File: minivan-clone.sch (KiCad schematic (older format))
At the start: 15 parts, among them CON101 HRO-TYPE-C-31-M-12, SW101 SW_PUSH, U101 ATMEGA32U2, X101 XTAL

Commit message: done work on mcu and started on matrix
done work on mcu and started on matrix
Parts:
- added C110: C, symbol keyboard_parts:C
- added CON101: CONN_3X2, symbol keyboard_parts:CONN_3X2
- added R102: 10K, symbol keyboard_parts:R
- added R103, R104: 22R, symbol keyboard_parts:R
- added R105, R106: 5K1, symbol keyboard_parts:R
- CON101: footprint (none) -> Type-C:HRO-TYPE-C-31-M-12-HandSoldering
- R101: value R -> 10K
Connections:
- net labels added: DN, DP, MISO, MOSI, PB0, PB1, PB2, PB3, PB4, PB5, PB6, PB7, PC2, PC4, PC5, PC6, PC7, PD0, PD1, PD2, PD3, PD4, PD5, PD6, RST, RX, SCK, TX
- wire segments 23 -> 61
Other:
- note added: "Dubbelkolla så denna ska va pulldown\n"
- moved on the sheet: C109, PTC101, R101, SW101

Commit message: started doing layout
started doing layout
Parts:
- removed X101: XTAL, symbol keyboard_parts:XTAL
- added D148: PRTR5V0U2X, Package_TO_SOT_SMD:SOT-143, symbol Power_Protection:PRTR5V0U2X
- added X101: XTAL_GND, keyboard_parts:FA-238, symbol keyboard_parts:XTAL_GND
- C101, C102, C103, C104, C109: value C -> 0,1uF; footprint (none) -> keyboard_parts:C_1608_rev2
- C105, C106: value C -> 4,7uF; footprint (none) -> keyboard_parts:C_3216_rev2
- C107, C108: value C -> C_xtal; footprint (none) -> keyboard_parts:C_1608_rev2
- C110: value C -> 1uF; footprint (none) -> keyboard_parts:C_3216_rev2
- CON102: renamed from CON101; footprint (none) -> keyboard_parts:AVR_ICSP_3x2
- PTC101: footprint (none) -> keyboard_parts:C_3216_rev2
- R101, R102, R103, R104, R105, R106: footprint (none) -> keyboard_parts:R_1608_rev2
- SW101: footprint (none) -> keyboard_parts:SW_ALPS_SKRP
- U101: footprint (none) -> keyboard_parts:QFP32
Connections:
- net labels added: D+, D-
- wire segments 61 -> 82
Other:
- note added: "Dubbelkolla kapacitans"
- note removed: "Dubbelkolla så denna ska va pulldown\n"
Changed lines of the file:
@@
 F 0 "U101" H 7925 2837 60  0000 C CNN
 F 1 "ATMEGA32U2" H 7925 2731 60  0000 C CNN
-F 2 "" H 7900 1500 60  0000 C CNN
+F 2 "keyboard_parts:QFP32" H 7900 1500 60  0001 C CNN
 F 3 "" H 7900 1500 60  0000 C CNN
 	1    7900 1800
-	1    0    0    -1
-$EndComp
-$Comp
-L keyboard_parts:XTAL X101
-U 1 1 5D1B97DB
-P 5050 1300
-F 0 "X101" H 5050 1592 60  0000 C CNN
-F 1 "XTAL" H 5050 1486 60  0000 C CNN
-F 2 "" H 5050 1300 60  0000 C CNN
-F 3 "" H 5050 1300 60  0000 C CNN
-	1    5050 1300
 	1    0    0    -1
 $EndComp
@@
 F 0 "SW101" H 10600 2105 50  0000 C CNN
 F 1 "SW_PUSH" H 10600 2014 50  0000 C CNN
-F 2 "" H 10600 1850 60  0000 C CNN
+F 2 "keyboard_parts:SW_ALPS_SKRP" H 10600 1850 60  0001 C CNN
 F 3 "" H 10600 1850 60  0000 C CNN
 	1    10600 1850
@@
 F 0 "R101" H 10371 1596 50  0000 L CNN
 F 1 "10K" H 10371 1505 50  0000 L CNN
-F 2 "" H 10300 1550 60  0000 C CNN
+F 2 "keyboard_parts:R_1608_rev2" H 10300 1550 60  0001 C CNN
 F 3 "" H 10300 1550 60  0000 C CNN
 	1    10300 1550
@@
 P 9100 5700
 F 0 "C102" H 9230 5746 50  0000 L CNN
-F 1 "C" H 9230 5655 50  0000 L CNN
-F 2 "" H 9100 5700 60  0000 C CNN
+F 1 "0,1uF" H 9230 5655 50  0000 L CNN
+F 2 "keyboard_parts:C_1608_rev2" H 9100 5700 60  0001 C CNN
 F 3 "" H 9100 5700 60  0000 C CNN
 	1    9100 5700
@@
 P 8500 5700
 F 0 "C101" H 8630 5746 50  0000 L CNN
-F 1 "C" H 8630 5655 50  0000 L CNN
-F 2 "" H 8500 5700 60  0000 C CNN
+F 1 "0,1uF" H 8630 5655 50  0000 L CNN
+F 2 "keyboard_parts:C_1608_rev2" H 8500 5700 60  0001 C CNN
 F 3 "" H 8500 5700 60  0000 C CNN
 	1    8500 5700
@@
 P 9600 5700
 F 0 "C103" H 9730 5746 50  0000 L CNN
-F 1 "C" H 9730 5655 50  0000 L CNN
-F 2 "" H 9600 5700 60  0000 C CNN
+F 1 "0,1uF" H 9730 5655 50  0000 L CNN
+F 2 "keyboard_parts:C_1608_rev2" H 9600 5700 60  0001 C CNN
 F 3 "" H 9600 5700 60  0000 C CNN
 	1    9600 5700
@@
 P 10100 5700
 F 0 "C104" H 10230 5746 50  0000 L CNN
-F 1 "C" H 10230 5655 50  0000 L CNN
-F 2 "" H 10100 5700 60  0000 C CNN
+F 1 "0,1uF" H 10230 5655 50  0000 L CNN
+F 2 "keyboard_parts:C_1608_rev2" H 10100 5700 60  0001 C CNN
 F 3 "" H 10100 5700 60  0000 C CNN
 	1    10100 5700
@@
 P 7350 5700
 F 0 "C105" H 7480 5746 50  0000 L CNN
-F 1 "C" H 7480 5655 50  0000 L CNN
-F 2 "" H 7350 5700 60  0000 C CNN
+F 1 "4,7uF" H 7480 5655 50  0000 L CNN
+F 2 "keyboard_parts:C_3216_rev2" H 7350 5700 60  0001 C CNN
 F 3 "" H 7350 5700 60  0000 C CNN
 	1    7350 5700
@@
 P 6200 5700
 F 0 "C106" H 6330 5746 50  0000 L CNN
-F 1 "C" H 6330 5655 50  0000 L CNN
-F 2 "" H 6200 5700 60  0000 C CNN
+F 1 "4,7uF" H 6330 5655 50  0000 L CNN
+F 2 "keyboard_parts:C_3216_rev2" H 6200 5700 60  0001 C CNN
 F 3 "" H 6200 5700 60  0000 C CNN
 	1    6200 5700
@@
 P 4750 1600
 F 0 "C107" H 4880 1646 50  0000 L CNN
-F 1 "C" H 4880 1555 50  0000 L CNN
-F 2 "" H 4750 1600 60  0000 C CNN
+F 1 "C_xtal" H 4880 1555 50  0000 L CNN
+F 2 "keyboard_parts:C_1608_rev2" H 4750 1600 60  0001 C CNN
 F 3 "" H 4750 1600 60  0000 C CNN
 	1    4750 1600
@@
 P 5350 1600
 F 0 "C108" H 5480 1646 50  0000 L CNN
-F 1 "C" H 5480 1555 50  0000 L CNN
-F 2 "" H 5350 1600 60  0000 C CNN
+F 1 "C_xtal" H 5480 1555 50  0000 L CNN
+F 2 "keyboard_parts:C_1608_rev2" H 5350 1600 60  0001 C CNN
 F 3 "" H 5350 1600 60  0000 C CNN
 	1    5350 1600
 	1    0    0    -1
 $EndComp
-Wire Wire Line
-	5350 1300 5350 1400
-Wire Wire Line
-	4750 1300 4750 1400
 $Comp
 L keyboard_parts:C C109
@@
 P 10300 2150
 F 0 "C109" H 10430 2196 50  0000 L CNN
-F 1 "C" H 10430 2105 50  0000 L CNN
-F 2 "" H 10300 2150 60  0000 C CNN
+F 1 "0,1uF" H 10430 2105 50  0000 L CNN
+F 2 "keyboard_parts:C_1608_rev2" H 10300 2150 60  0001 C CNN
 F 3 "" H 10300 2150 60  0000 C CNN
 	1    10300 2150
@@
 	6850 1050 4750 1050
 Wire Wire Line
-	4750 1050 4750 1300
-Connection ~ 4750 1300
-Wire Wire Line
 	6850 1150 5350 1150
-Wire Wire Line
-	5350 1150 5350 1300
-Connection ~ 5350 1300
 Connection ~ 8500 5900
 Wire Wire Line
@@
 F 0 "R102" H 5921 2546 50  0000 L CNN
 F 1 "10K" H 5921 2455 50  0000 L CNN
-F 2 "" H 5850 2500 60  0000 C CNN
+F 2 "keyboard_parts:R_1608_rev2" H 5850 2500 60  0001 C CNN
 F 3 "" H 5850 2500 60  0000 C CNN
 	1    5850 2500
@@
 	1    0    0    -1
 $EndComp
-Text Notes 5200 2900 0    50   ~ 0
-Dubbelkolla så denna ska va pulldown\n
 $Comp
 L keyboard_parts:+5V #PWR0109
@@
 P 9900 1350
 F 0 "C110" H 10030 1396 50  0000 L CNN
-F 1 "C" H 10030 1305 50  0000 L CNN
-F 2 "" H 9900 1350 60  0000 C CNN
+F 1 "1uF" H 10030 1305 50  0000 L CNN
+F 2 "keyboard_parts:C_3216_rev2" H 9900 1350 60  0001 C CNN
 F 3 "" H 9900 1350 60  0000 C CNN
 	1    9900 1350
@@
 	2200 2250 1950 2250
 Text Label 3900 1950 0    50   ~ 0
-DN
+D+
 Text Label 3950 2050 0    50   ~ 0
-DP
+D-
 Wire Wire Line
 	1950 1650 2500 1650
@@
 F 0 "R104" H 3271 1996 50  0000 L CNN
 F 1 "22R" H 3271 1905 50  0000 L CNN
-F 2 "" H 3200 1950 60  0000 C CNN
+F 2 "keyboard_parts:R_1608_rev2" H 3200 1950 60  0001 C CNN
 F 3 "" H 3200 1950 60  0000 C CNN
 	1    3200 1950
@@
 F 0 "R103" H 3671 2096 50  0000 L CNN
 F 1 "22R" H 3671 2005 50  0000 L CNN
-F 2 "" H 3600 2050 60  0000 C CNN
+F 2 "keyboard_parts:R_1608_rev2" H 3600 2050 60  0001 C CNN
 F 3 "" H 3600 2050 60  0000 C CNN
 	1    3600 2050
@@
 F 0 "R106" H 2771 2896 50  0000 L CNN
 F 1 "5K1" H 2771 2805 50  0000 L CNN
-F 2 "" H 2700 2850 60  0000 C CNN
+F 2 "keyboard_parts:R_1608_rev2" H 2700 2850 60  0001 C CNN
 F 3 "" H 2700 2850 60  0000 C CNN
 	1    2700 2850
@@
 F 0 "R105" H 2371 2896 50  0000 L CNN
 F 1 "5K1" H 2371 2805 50  0000 L CNN
-F 2 "" H 2300 2850 60  0000 C CNN
+F 2 "keyboard_parts:R_1608_rev2" H 2300 2850 60  0001 C CNN
 F 3 "" H 2300 2850 60  0000 C CNN
 	1    2300 2850
@@
 DP
 $Comp
-L keyboard_parts:CONN_3X2 CON101
+L keyboard_parts:CONN_3X2 CON102
 U 1 1 5D216CCA
 P 7700 3950
-F 0 "CON101" H 7700 4250 50  0000 C CNN
+F 0 "CON102" H 7700 4250 50  0000 C CNN
 F 1 "CONN_3X2" H 7700 4166 40  0000 C CNN
-F 2 "" H 7700 3900 60  0000 C CNN
+F 2 "keyboard_parts:AVR_ICSP_3x2" H 7700 3900 60  0001 C CNN
 F 3 "" H 7700 3900 60  0000 C CNN
 	1    7700 3950
@@
 F 0 "PTC101" H 2750 1965 50  0000 C CNN
 F 1 "PTC" H 2750 1874 50  0000 C CNN
-F 2 "" V 2750 1650 60  0000 C CNN
+F 2 "keyboard_parts:C_3216_rev2" V 2750 1650 60  0001 C CNN
 F 3 "" V 2750 1650 60  0000 C CNN
 	1    2750 1650
 	1    0    0    -1
 $EndComp
+Text Label 2750 4500 0    50   ~ 0
+PC2
+Text Label 2750 4600 0    50   ~ 0
+PD0
+Text Label 2750 4700 0    50   ~ 0
+PD1
+Text Label 2750 4900 0    50   ~ 0
+PD4
+Text Label 2750 5000 0    50   ~ 0
+PD5
+Text Label 2750 5100 0    50   ~ 0
+PD6
+Text Label 2750 5200 0    50   ~ 0
+PB0
+Text Label 2750 5600 0    50   ~ 0
+PB4
+Text Label 2750 5700 0    50   ~ 0
+PB5
+Text Label 2750 5800 0    50   ~ 0
+PB6
+Text Label 2750 5900 0    50   ~ 0
+PC6
+Text Label 2750 6000 0    50   ~ 0
+PC5
+Text Label 2750 6100 0    50   ~ 0
+PC4
+Text Label 2750 5300 0    50   ~ 0
+PB1
+Text Label 2750 5400 0    50   ~ 0
+PB2
+Text Label 2750 5500 0    50   ~ 0
+PB3
+Text Label 2750 4800 0    50   ~ 0
+PD2
+Wire Wire Line
+	2750 4500 2650 4500
+Wire Wire Line
+	2750 4600 2650 4600
+Wire Wire Line
+	2750 4700 2650 4700
+Wire Wire Line
+	2750 4800 2650 4800
+Wire Wire Line
+	2750 4900 2650 4900
+Wire Wire Line
+	2650 5000 2750 5000
+Wire Wire Line
+	2650 5100 2750 5100
+Wire Wire Line
+	2650 5200 2750 5200
+Wire Wire Line
+	2650 5300 2750 5300
+Wire Wire Line
+	2650 5400 2750 5400
+Wire Wire Line
+	2650 5500 2750 5500
+Wire Wire Line
+	2650 5600 2750 5600
+Wire Wire Line
+	2650 5700 2750 5700
+Wire Wire Line
+	2650 5800 2750 5800
+Wire Wire Line
+	2650 5900 2750 5900
+Wire Wire Line
+	2650 6000 2750 6000
+Wire Wire Line
+	2650 6100 2750 6100
+Text Notes 4850 2100 0    50   ~ 0
+Dubbelkolla kapacitans
+$Comp
+L Power_Protection:PRTR5V0U2X D148
+U 1 1 5D2462AC
+P 4550 3750
+F 0 "D148" H 5094 3796 50  0000 L CNN
+F 1 "PRTR5V0U2X" H 5094 3705 50  0000 L CNN
+F 2 "Package_TO_SOT_SMD:SOT-143" H 4610 3750 50  0001 C CNN
+F 3 "https://assets.nexperia.com/documents/data-sheet/PRTR5V0U2X.pdf" H 4610 3750 50  0001 C CNN
+	1    4550 3750
+	1    0    0    -1
+$EndComp
+$Comp
+L keyboard_parts:+5V #PWR0120
+U 1 1 5D246C4B
+P 4550 3250
+F 0 "#PWR0120" H 4550 3220 20  0001 C CNN
+F 1 "+5V" H 4550 3388 30  0000 C CNN
+F 2 "" H 4550 3250 60  0000 C CNN
+F 3 "" H 4550 3250 60  0000 C CNN
+	1    4550 3250
+	1    0    0    -1
+$EndComp
+$Comp
+L keyboard_parts:GND #PWR0121
+U 1 1 5D24743D
+P 4550 4250
+F 0 "#PWR0121" H 4550 4300 20  0001 C CNN
+F 1 "GND" H 4550 4309 30  0000 C CNN
+F 2 "" H 4550 4250 60  0000 C CNN
+F 3 "" H 4550 4250 60  0000 C CNN
+	1    4550 4250
+	1    0    0    -1
+$EndComp
+Text Label 5050 3600 0    50   ~ 0
+D+
+Text Label 4050 3600 0    50   ~ 0
+D-
+Wire Wire Line
+	4050 3600 4050 3750
+Wire Wire Line
+	5050 3600 5050 3750
+$Comp
+L keyboard_parts:XTAL_GND X101
+U 1 1 5D25544A
+P 5050 1250
+F 0 "X101" H 5050 1542 60  0000 C CNN
+F 1 "XTAL_GND" H 5050 1436 60  0000 C CNN
+F 2 "keyboard_parts:FA-238" H 5050 1250 60  0001 C CNN
+F 3 "" H 5050 1250 60  0000 C CNN
+	1    5050 1250
+	1    0    0    -1
+$EndComp
+Wire Wire Line
+	4750 1050 4750 1250
+Wire Wire Line
+	5350 1150 5350 1250
+Connection ~ 4750 1250
+Wire Wire Line
+	4750 1250 4750 1400
+Connection ~ 5350 1250
+Wire Wire Line
+	5350 1250 5350 1400
+Wire Wire Line
+	5050 1450 5050 1800
+Wire Wire Line
+	5050 1800 4750 1800
+Connection ~ 4750 1800
 $EndSCHEMATC

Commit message: fixed row 2
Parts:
- CON101: symbol Type-C:HRO-TYPE-C-31-M-12 -> minivan-clone-rescue:HRO-TYPE-C-31-M-12-Type-C
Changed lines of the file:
@@
 EESchema Schematic File Version 4
 LIBS:minivan-clone-cache
-EELAYER 29 0
+EELAYER 30 0
 EELAYER END
 $Descr A4 11693 8268
@@
 $EndComp
 $Comp
-L Type-C:HRO-TYPE-C-31-M-12 CON101
+L minivan-clone-rescue:HRO-TYPE-C-31-M-12-Type-C CON101
 U 1 1 5D1BD550
 P 1850 2100

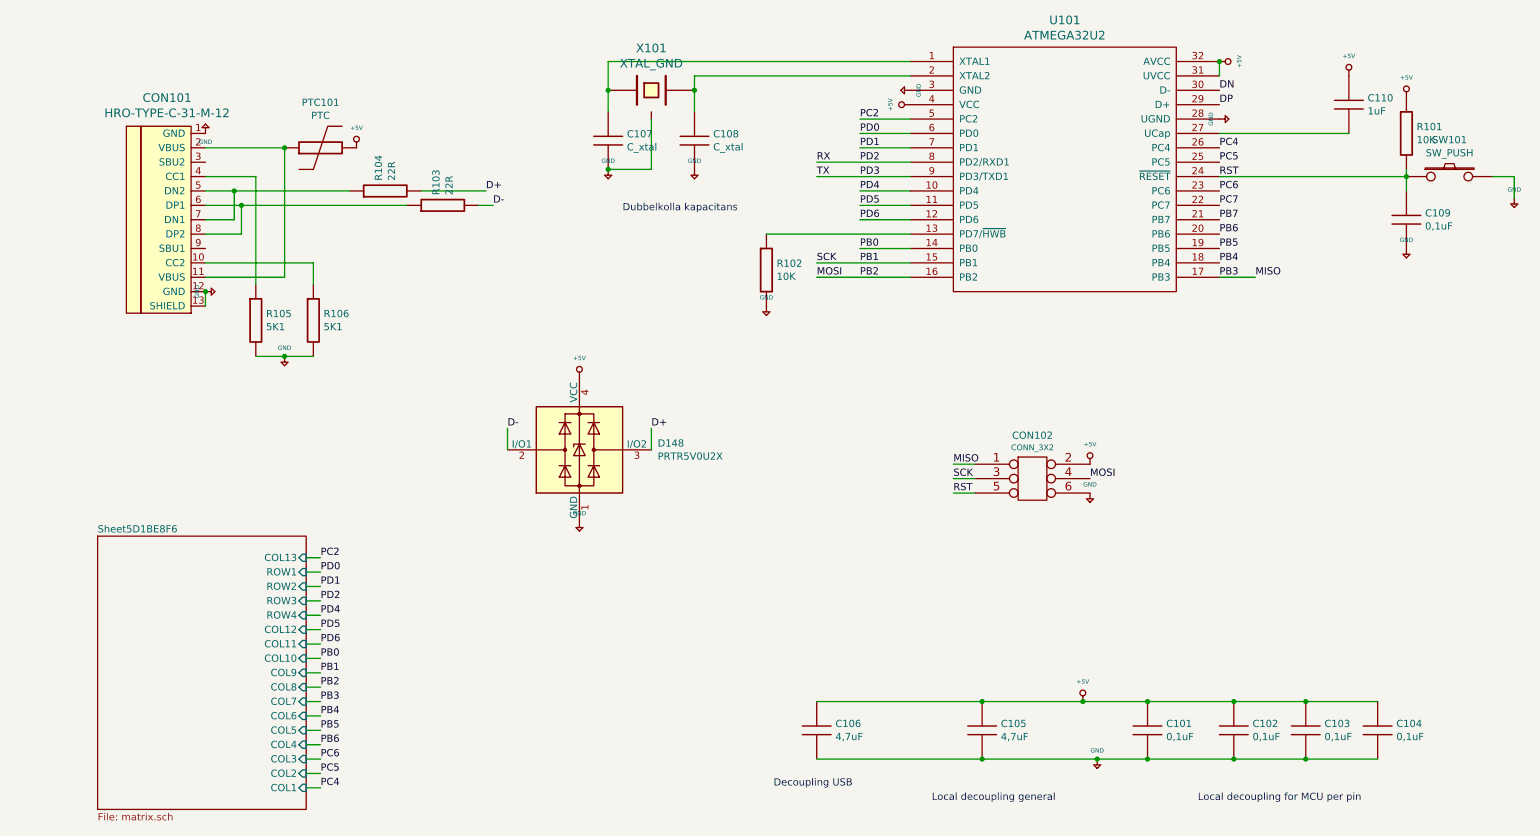
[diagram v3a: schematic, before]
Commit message: removed ICSP, fixed gnd and 5v
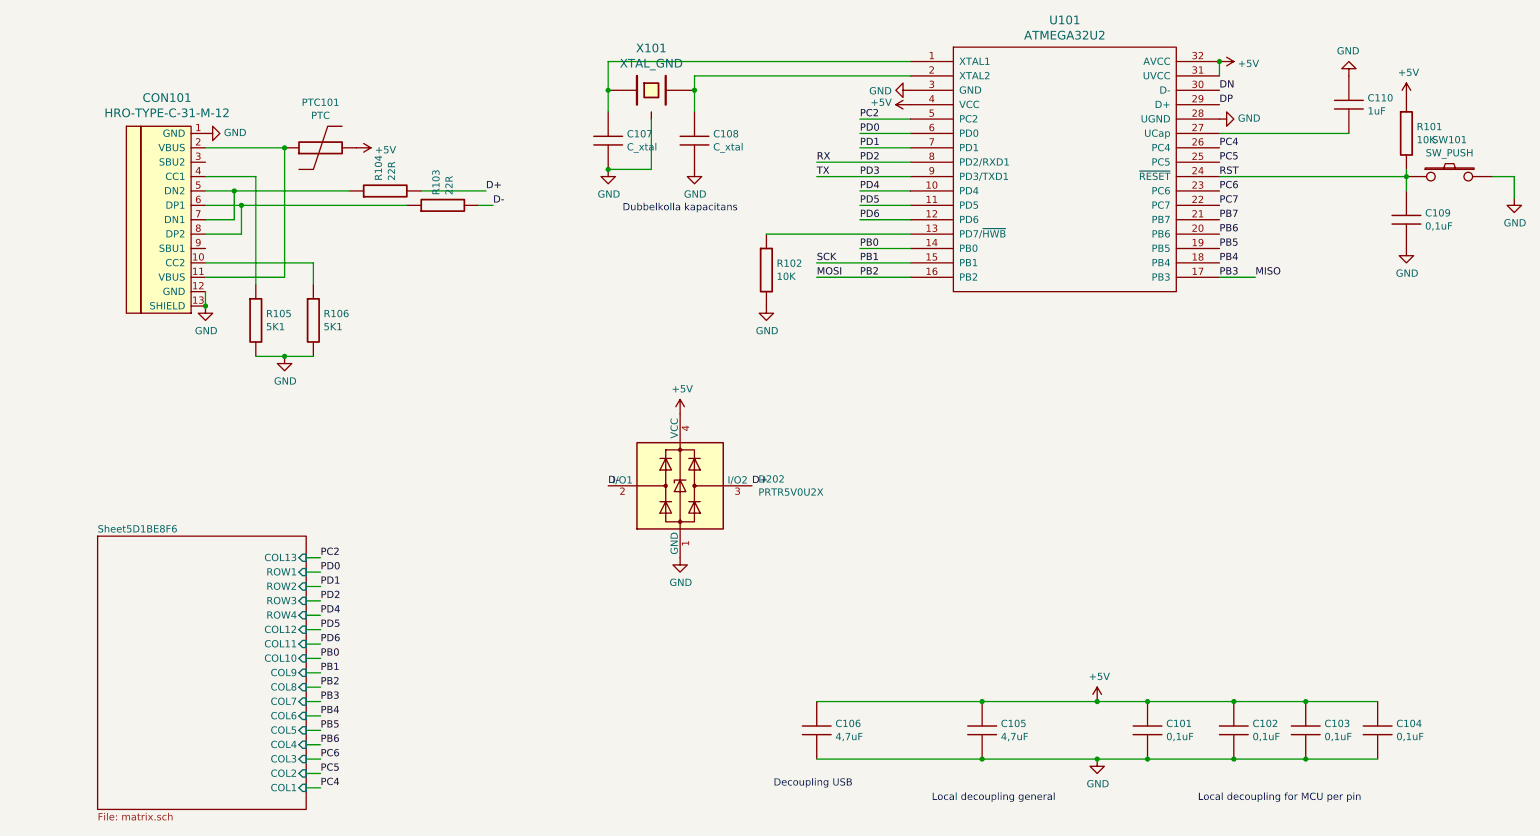
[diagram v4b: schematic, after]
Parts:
- removed CON102: CONN_3X2, keyboard_parts:AVR_ICSP_3x2, symbol keyboard_parts:CONN_3X2
- removed D148: PRTR5V0U2X, Package_TO_SOT_SMD:SOT-143, symbol Power_Protection:PRTR5V0U2X
- added D202: PRTR5V0U2X, Package_TO_SOT_SMD:SOT-143, symbol Power_Protection:PRTR5V0U2X
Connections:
- net +5V: now also D202.4 (VCC); no longer C101.2, C102.2, C103.2, C104.2, C105.2, C106.2, C107.2, C108.2, C109.2, C110.1, CON101.1 (GND), CON101.12 (GND), CON101.13 (SHIELD), R102.2, R105.2, R106.2, SW101.2, U101.28 (UGND), U101.3 (GND), X101.3
- net D+: now also D202.3 (I/O2)
- net D-: now also D202.2 (I/O1)
- new net GND: C101.2, C102.2, C103.2, C104.2, C105.2, C106.2, C107.2, C108.2, C109.2, C110.1, CON101.1 (GND), CON101.12 (GND), CON101.13 (SHIELD), D202.1 (GND), R102.2, R105.2, R106.2, SW101.2, U101.28 (UGND), U101.3 (GND), X101.3

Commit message: Started routing
Started routing
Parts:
- removed C104: 0,1uF, keyboard_parts:C_1608_rev2, symbol keyboard_parts:C
- CON101: symbol minivan-clone-rescue:HRO-TYPE-C-31-M-12-Type-C -> minivan-clone-rescue:HRO-TYPE-C-31-M-12-Type-C-minivan-clone-rescue
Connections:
- net labels added: pre_D+, pre_D-
- net labels removed: DN, DP, MISO, MOSI, RX, SCK, TX
- wire segments 77 -> 75
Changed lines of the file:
@@
 EESchema Schematic File Version 4
 LIBS:minivan-clone-cache
-EELAYER 30 0
+EELAYER 29 0
 EELAYER END
 $Descr A4 11693 8268
@@
 	1    0    0    -1
 $EndComp
-$Comp
-L keyboard_parts:C C104
-U 1 1 5D1C40AA
-P 10100 5700
-F 0 "C104" H 10230 5746 50  0000 L CNN
-F 1 "0,1uF" H 10230 5655 50  0000 L CNN
-F 2 "keyboard_parts:C_1608_rev2" H 10100 5700 60  0001 C CNN
-F 3 "" H 10100 5700 60  0000 C CNN
-	1    10100 5700
-	1    0    0    -1
-$EndComp
 Text Notes 8850 6200 0    50   ~ 0
 Local decoupling for MCU per pin
@@
 Wire Wire Line
 	11050 1850 11050 2000
-Wire Wire Line
-	10100 5500 9600 5500
 Connection ~ 7350 5500
 Wire Wire Line
@@
 Wire Wire Line
 	9100 5500 8500 5500
-Connection ~ 9600 5500
 Wire Wire Line
 	9600 5500 9100 5500
@@
 Wire Wire Line
 	9100 5900 9600 5900
-Connection ~ 9600 5900
-Wire Wire Line
-	9600 5900 10100 5900
 Wire Wire Line
 	10300 1800 10300 1850
@@
 PC4
 Text Label 9000 1250 0    50   ~ 0
-DN
+D-
 Text Label 9000 1350 0    50   ~ 0
-DP
-Text Label 9250 2550 0    50   ~ 0
-MISO
-Text Label 6200 2550 0    50   ~ 0
-MOSI
-Text Label 6200 2450 0    50   ~ 0
-SCK
+D+
 Text Label 9000 1850 0    50   ~ 0
 RST
@@
 Wire Wire Line
 	6500 1550 6850 1550
-Text Label 6200 1750 0    50   ~ 0
-RX
-Text Label 6200 1850 0    50   ~ 0
-TX
 Wire Wire Line
 	6200 1750 6850 1750
@@
 	1    0    0    -1
 $EndComp
+Text Label 2750 4900 0    50   ~ 0
+PC2
+Text Label 2750 5500 0    50   ~ 0
+PD0
+Text Label 2750 5300 0    50   ~ 0
+PD3
+Text Label 2750 5200 0    50   ~ 0
+PD4
+Text Label 2750 5100 0    50   ~ 0
+PD5
 Text Label 2750 4500 0    50   ~ 0
-PC2
-Text Label 2750 4600 0    50   ~ 0
-PD0
-Text Label 2750 4700 0    50   ~ 0
-PD1
-Text Label 2750 4900 0    50   ~ 0
-PD4
+PD6
 Text Label 2750 5000 0    50   ~ 0
-PD5
-Text Label 2750 5100 0    50   ~ 0
-PD6
-Text Label 2750 5200 0    50   ~ 0
 PB0
 Text Label 2750 5600 0    50   ~ 0
@@
 Text Label 2750 6100 0    50   ~ 0
 PC4
-Text Label 2750 5300 0    50   ~ 0
+Text Label 2750 4700 0    50   ~ 0
 PB1
+Text Label 2750 4600 0    50   ~ 0
+PB3
 Text Label 2750 5400 0    50   ~ 0
-PB2
-Text Label 2750 5500 0    50   ~ 0
-PB3
-Text Label 2750 4800 0    50   ~ 0
 PD2
 Wire Wire Line
@@
 Wire Wire Line
 	2650 5300 2750 5300
-Wire Wire Line
-	2650 5400 2750 5400
 Wire Wire Line
 	2650 5500 2750 5500
@@
 	1950 2750 1950 2650
 $Comp
-L minivan-clone-rescue:HRO-TYPE-C-31-M-12-Type-C CON101
+L minivan-clone-rescue:HRO-TYPE-C-31-M-12-Type-C-minivan-clone-rescue CON101
 U 1 1 5D1BD550
 P 1850 2100
@@
 	1    0    0    -1
 $EndComp
+Text Label 5750 4000 0    50   ~ 0
+pre_D-
 Text Label 4750 4000 0    50   ~ 0
-D-
-Text Label 5750 4000 0    50   ~ 0
-D+
-$Comp
-L power:+5V #PWR?
+pre_D+
+$Comp
+L power:+5V #PWR0102
 U 1 1 5D78AA14
 P 5250 3500
-F 0 "#PWR?" H 5250 3350 50  0001 C CNN
+F 0 "#PWR0102" H 5250 3350 50  0001 C CNN
 F 1 "+5V" H 5265 3673 50  0000 C CNN
 F 2 "" H 5250 3500 50  0001 C CNN
@@
 $EndComp
 $Comp
-L power:+5V #PWR?
+L power:+5V #PWR0114
 U 1 1 5D78B5BE
 P 3000 1650
-F 0 "#PWR?" H 3000 1500 50  0001 C CNN
+F 0 "#PWR0114" H 3000 1500 50  0001 C CNN
 F 1 "+5V" V 3015 1778 50  0000 L CNN
 F 2 "" H 3000 1650 50  0001 C CNN
@@
 $EndComp
 $Comp
-L power:+5V #PWR?
+L power:+5V #PWR0115
 U 1 1 5D78C361
 P 6850 1350
-F 0 "#PWR?" H 6850 1200 50  0001 C CNN
+F 0 "#PWR0115" H 6850 1200 50  0001 C CNN
 F 1 "+5V" V 6865 1478 50  0000 L CNN
 F 2 "" H 6850 1350 50  0001 C CNN
@@
 $EndComp
 $Comp
-L power:+5V #PWR?
+L power:+5V #PWR0116
 U 1 1 5D78C75A
 P 9000 1050
-F 0 "#PWR?" H 9000 900 50  0001 C CNN
+F 0 "#PWR0116" H 9000 900 50  0001 C CNN
 F 1 "+5V" V 9015 1178 50  0000 L CNN
 F 2 "" H 9000 1050 50  0001 C CNN
@@
 Connection ~ 9000 1050
 $Comp
-L power:GND #PWR?
+L power:GND #PWR0117
 U 1 1 5D792811
 P 9000 1450
-F 0 "#PWR?" H 9000 1200 50  0001 C CNN
+F 0 "#PWR0117" H 9000 1200 50  0001 C CNN
 F 1 "GND" V 9005 1322 50  0000 R CNN
 F 2 "" H 9000 1450 50  0001 C CNN
@@
 $EndComp
 $Comp
-L power:+5V #PWR?
+L power:+5V #PWR0118
 U 1 1 5D792F03
 P 10300 1300
-F 0 "#PWR?" H 10300 1150 50  0001 C CNN
+F 0 "#PWR0118" H 10300 1150 50  0001 C CNN
 F 1 "+5V" H 10315 1473 50  0000 C CNN
 F 2 "" H 10300 1300 50  0001 C CNN
@@
 $EndComp
 $Comp
-L power:+5V #PWR?
+L power:+5V #PWR0119
 U 1 1 5D793283
 P 8150 5500
-F 0 "#PWR?" H 8150 5350 50  0001 C CNN
+F 0 "#PWR0119" H 8150 5350 50  0001 C CNN
 F 1 "+5V" H 8165 5673 50  0000 C CNN
 F 2 "" H 8150 5500 50  0001 C CNN
@@
 Wire Wire Line
 	8150 5500 8500 5500
+Text Label 2600 2050 0    50   ~ 0
+pre_D-
+Text Label 2600 1950 0    50   ~ 0
+pre_D+
+Wire Wire Line
+	2650 5400 2750 5400
+Text Label 2750 4800 0    50   ~ 0
+PB2
 $EndSCHEMATC
